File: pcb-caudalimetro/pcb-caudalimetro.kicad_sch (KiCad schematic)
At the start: 23 parts, among them J1 VCC, J2 SNTP_LED, J3 WIFI_LED, J4 FLASH_LED, J6 LAN, J7 PROG, J8 CAUDALIMETRO, SW1 EN, U1 ESP32-WROOM-32, U2 AMS1117-3.3, U3 LM7805_TO220, U4 ULN2003

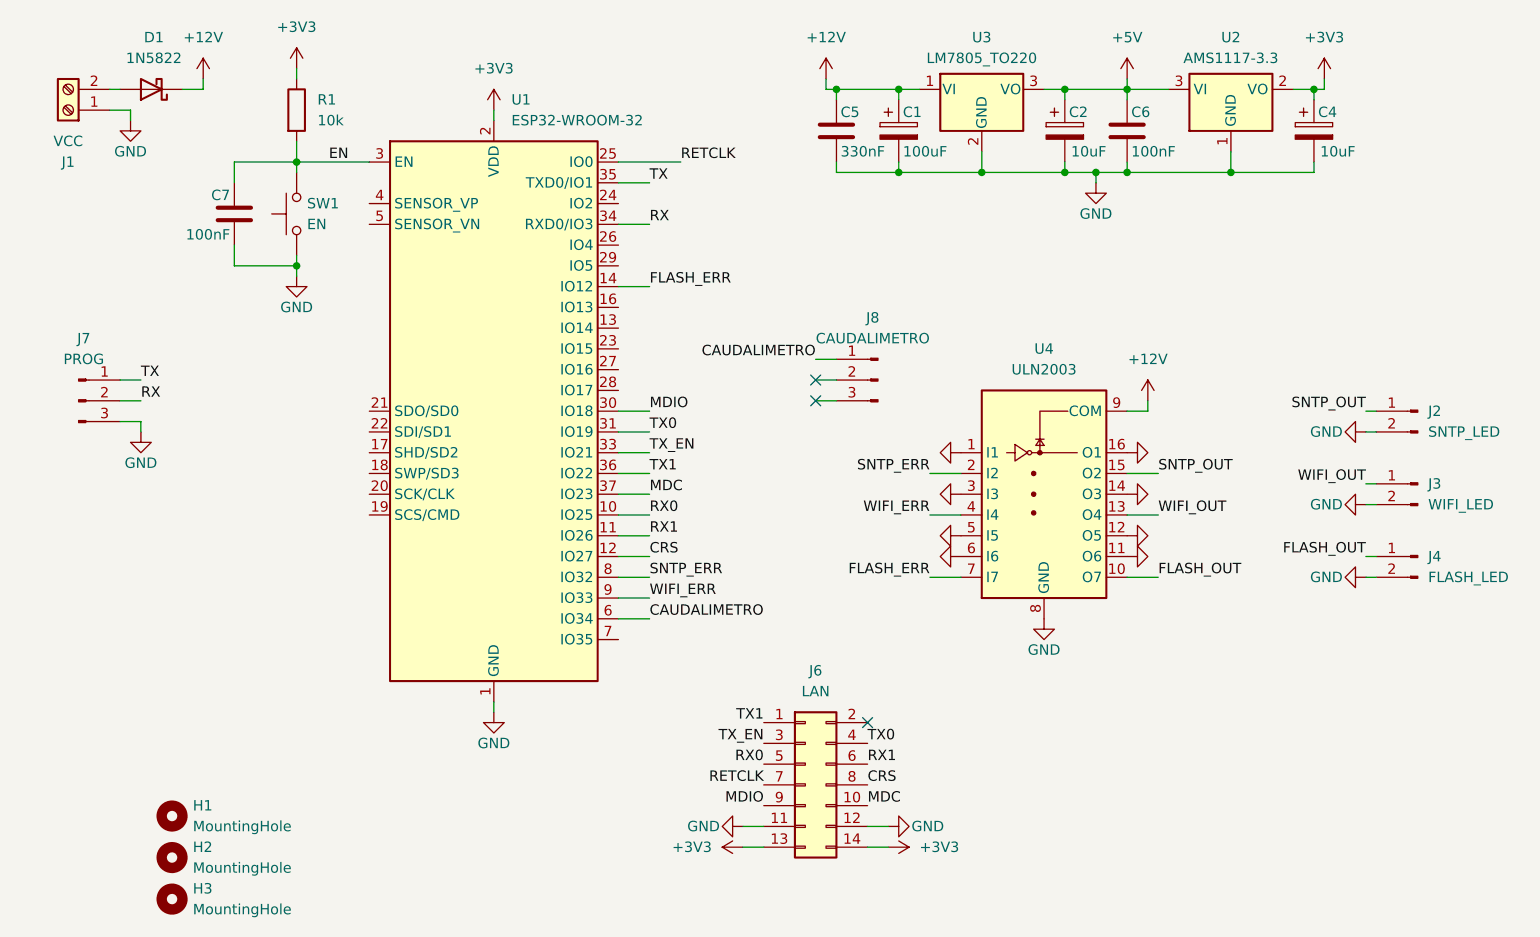
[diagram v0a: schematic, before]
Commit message: fix: add pull up en gpio input only
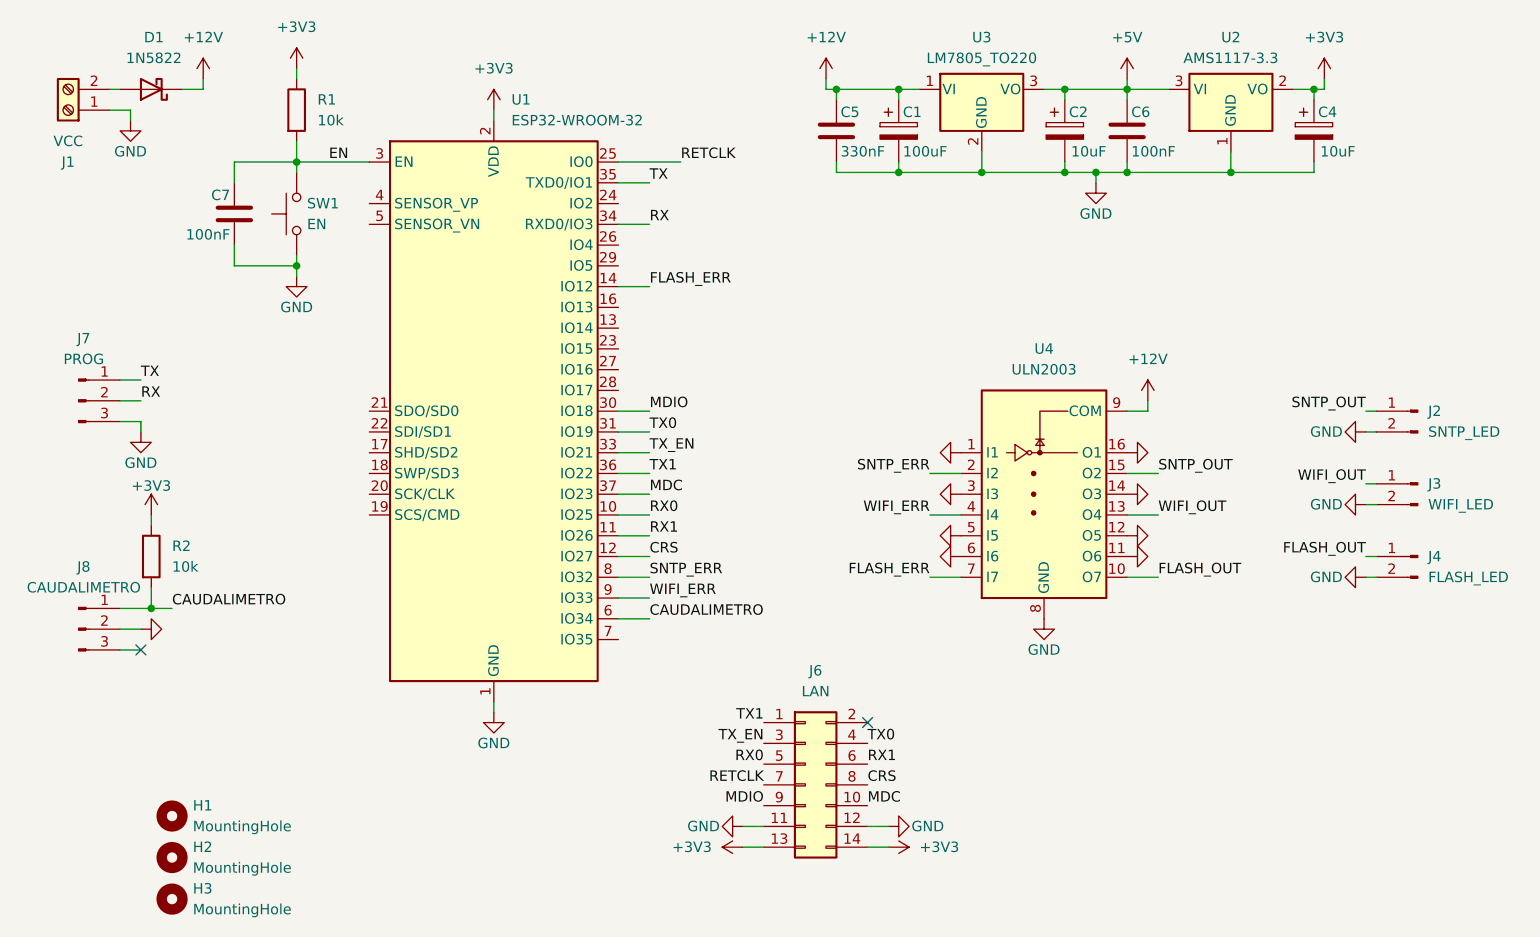
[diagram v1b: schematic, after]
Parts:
- added R2: 10k, Resistor_SMD:R_1206_3216Metric_Pad1.30x1.75mm_HandSolder, symbol Device:R
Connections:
- net +3V3: now also R2.1
- net CAUDALIMETRO: now also R2.2
- net GND: now also J8.2 (Pin_2)
- no-connect marks 3 -> 2
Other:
- moved on the sheet: J8

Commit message: feat: gerbers para grabado laser
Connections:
- net CAUDALIMETRO: now also U1.13 (IO14); no longer U1.6 (IO34)
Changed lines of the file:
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@@
 	(wire
 		(pts
-			(xy 88.9 88.9) (xy 92.71 88.9)
+			(xy 88.9 53.34) (xy 92.71 53.34)
 		)
 		(stroke
@@
 	)
 	(label "CAUDALIMETRO"
-		(at 92.71 88.9 0)
-		(effects
-			(font
+		(at 92.71 53.34 0)
+		(effects
+			(font

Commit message: chore: generar gerbers y BOM
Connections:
- net GND: no longer U4.11 (O6), U4.12 (O5), U4.14 (O3), U4.16 (O1)
